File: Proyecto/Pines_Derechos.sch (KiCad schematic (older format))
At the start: 6 parts, among them U1 MAX7219, U2 MAX7219

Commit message: Avance de FootPrints
Se terminó diseño de esquemáticos en ojas Jerárquicas; se avanzó a un
70% en las referencias de FootPrint, y se actualizaron hojas de datos de
la Matriz de LEDs 8x8.
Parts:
- added M1: Matrix_8x8_LED, symbol Matrix_8x8_LED
- AFF1: footprint (none) -> FootPrints:Cx56-12
- R1, R2: footprint (none) -> FootPrints:R_0805_HandSoldering
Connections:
- net labels added: PF
- net labels removed: +3.3V
- wire segments 84 -> 95
- no-connect marks 30 -> 31
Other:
- note added: "Power Flag\ncon etiqueta global."

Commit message: Modelos 3D
Se modificaron FootPrints y se agregaron modelos en 3D.
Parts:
- AFF1: Desc (none) -> Character LED Display Module Red 7-Segment 4 Character Comm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; Digikey# (none) -> 67-1442-ND; Manf (none) -> Lumex Opto/Components Inc.; Manf# (none) -> LDQ-N514RI
- M1: footprint (none) -> FootPrints:Matrix_8x8_LEDs; Desc (none) -> Dot Matrix Display Module 8 x 8 Common Cathode Row, Common 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; Digikey# (none) -> TA15-11EWA-ND; Manf (none) -> Kingbright; Manf# (none) -> TA15-11EWA
- R1, R2: Desc (none) -> Resistencia en microprocesador 0.25 W, 1/4 W ±0.5% 9.53 k O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; Digikey# (none) -> P21131TR-ND; Manf (none) -> Panasonic Electronic Components; Manf# (none) -> ERJ-PB6D9531V
- U1, U2: footprint (none) -> FootPrints:MAX7219; Desc (none) -> IC DRIVER LED DISP 8DGT 24-SOIC; Digikey# (none) -> MAX7219CWG+-ND; Manf (none) -> Maxim Integrated; Manf# (none) -> MAX7219CWG+
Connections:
- net labels removed: PF
- wire segments 95 -> 94
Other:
- note added: "En los Integrados MAX7219:\nLos cátodos son - DIG0 al DIG 7.\nLos ánodos son SEGa al SEGg y SEGdp"
- note removed: "Power Flag\ncon etiqueta global."
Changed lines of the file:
@@
 F 0 "U1" H 2350 3600 50  0000 C CNN
 F 1 "MAX7219" H 3050 3600 50  0000 C CNN
-F 2 "" H 2750 2800 50  0001 C CNN
-F 3 "" H 2750 2800 50  0001 C CNN
+F 2 "FootPrints:MAX7219" H 2750 2800 50  0001 C CNN
+F 3 "MAX7219,21" H 2750 2800 50  0001 C CNN
+F 4 "Maxim Integrated" H 2750 2800 60  0001 C CNN "Manf"
+F 5 "MAX7219CWG+" H 2750 2800 60  0001 C CNN "Manf#"
+F 6 "MAX7219CWG+-ND" H 2750 2800 60  0001 C CNN "Digikey#"
+F 7 "IC DRIVER LED DISP 8DGT 24-SOIC" H 2750 2800 60  0001 C CNN "Desc"
 	1    2750 2800
 	1    0    0    -1
@@
 F 1 "9.53k" V 4050 2850 50  0000 C CNN
 F 2 "FootPrints:R_0805_HandSoldering" V 3980 2850 50  0001 C CNN
-F 3 "" H 4050 2850 50  0001 C CNN
+F 3 "Fixed Resistors Prod Catalog" H 4050 2850 50  0001 C CNN
+F 4 "Panasonic Electronic Components" V 4050 2850 60  0001 C CNN "Manf"
+F 5 "ERJ-PB6D9531V" V 4050 2850 60  0001 C CNN "Manf#"
+F 6 "P21131TR-ND" V 4050 2850 60  0001 C CNN "Digikey#"
+F 7 "Resistencia en microprocesador 0.25 W, 1/4 W ±0.5% 9.53 k Ohm AEC-Q200 automotriz, protección contra impulsos Película gruesa 0805 (2012 métrico)" V 4050 2850 60  0001 C CNN "Desc"
 	1    4050 2850
 	0    1    1    0
@@
 F 1 "CA56-12" H 2800 5950 50  0000 C CNN
 F 2 "FootPrints:Cx56-12" H 2250 5250 50  0001 C CNN
-F 3 "" H 2250 5250 50  0001 C CNN
+F 3 "LDQ-N514RI" H 2250 5250 50  0001 C CNN
+F 4 "Lumex Opto/Components Inc." H 2750 5250 60  0001 C CNN "Manf"
+F 5 "LDQ-N514RI" H 2750 5250 60  0001 C CNN "Manf#"
+F 6 "67-1442-ND" H 2750 5250 60  0001 C CNN "Digikey#"
+F 7 "Character LED Display Module Red 7-Segment 4 Character Common Cathode 2V 10mA 0.748\" H x 1.980\" W x 0.315\" D (19.00mm x 50.30mm x 8.00mm) 12-DIP (0.600\", 15.24mm)" H 2750 5250 60  0001 C CNN "Desc"
 	1    2750 5250
 	1    0    0    -1
@@
 F 0 "U2" H 8500 3500 50  0000 C CNN
 F 1 "MAX7219" H 9200 3500 50  0000 C CNN
-F 2 "" H 8900 2700 50  0001 C CNN
-F 3 "" H 8900 2700 50  0001 C CNN
+F 2 "FootPrints:MAX7219" H 8900 2700 50  0001 C CNN
+F 3 "MAX7219,21" H 8900 2700 50  0001 C CNN
+F 4 "Maxim Integrated" H 8900 2700 60  0001 C CNN "Manf"
+F 5 "MAX7219CWG+" H 8900 2700 60  0001 C CNN "Manf#"
+F 6 "MAX7219CWG+-ND" H 8900 2700 60  0001 C CNN "Digikey#"
+F 7 "IC DRIVER LED DISP 8DGT 24-SOIC" H 8900 2700 60  0001 C CNN "Desc"
 	1    8900 2700
 	1    0    0    -1
@@
 F 1 "9.53k" V 10200 2750 50  0000 C CNN
 F 2 "FootPrints:R_0805_HandSoldering" V 10130 2750 50  0001 C CNN
-F 3 "" H 10200 2750 50  0001 C CNN
+F 3 "Fixed Resistors Prod Catalog" H 10200 2750 50  0001 C CNN
+F 4 "Panasonic Electronic Components" V 10200 2750 60  0001 C CNN "Manf"
+F 5 "ERJ-PB6D9531V" V 10200 2750 60  0001 C CNN "Manf#"
+F 6 "P21131TR-ND" V 10200 2750 60  0001 C CNN "Digikey#"
+F 7 "Resistencia en microprocesador 0.25 W, 1/4 W ±0.5% 9.53 k Ohm AEC-Q200 automotriz, protección contra impulsos Película gruesa 0805 (2012 métrico)" V 10200 2750 60  0001 C CNN "Desc"
 	1    10200 2750
 	0    1    1    0
@@
 L GND #PWR?
 U 1 1 59275BE8
-P 6100 7000
+P 6100 6850
 AR Path="/59275BE8" Ref="#PWR?"  Part="1"
 AR Path="/5926FB74/59275BE8" Ref="#PWR06"  Part="1"
-F 0 "#PWR06" H 6100 6750 50  0001 C CNN
-F 1 "GND" H 5950 6950 50  0000 C CNN
-F 2 "" H 6100 7000 50  0001 C CNN
-F 3 "" H 6100 7000 50  0001 C CNN
-	1    6100 7000
+F 0 "#PWR06" H 6100 6600 50  0001 C CNN
+F 1 "GND" H 5950 6800 50  0000 C CNN
+F 2 "" H 6100 6850 50  0001 C CNN
+F 3 "" H 6100 6850 50  0001 C CNN
+	1    6100 6850
 	1    0    0    -1
 $EndComp
@@
 Entry Wire Line
 	7450 3150 7550 3050
-Text Label 6100 6850 2    60   ~ 0
-GND
-Wire Wire Line
-	6100 6850 6100 7000
-Wire Notes Line
-	5750 6600 6350 6600
-Wire Notes Line
-	6350 6600 6350 7300
-Wire Notes Line
-	6350 7300 5750 7300
-Wire Notes Line
-	5750 7300 5750 6600
-Wire Notes Line
-	5750 7300 5550 7500
-Wire Notes Line
-	5550 7500 5400 7500
-Text Notes 4250 7600 0    60   ~ 0
+Wire Wire Line
+	6100 6700 6100 6850
+Wire Notes Line
+	5750 6450 6350 6450
+Wire Notes Line
+	6350 6450 6350 7150
+Wire Notes Line
+	6350 7150 5750 7150
+Wire Notes Line
+	5750 7150 5750 6450
+Wire Notes Line
+	5750 7150 5550 7350
+Wire Notes Line
+	5550 7350 5400 7350
+Text Notes 4250 7450 0    60   ~ 0
 GND con etiqueta global\npara el MAX7219 de la \nmatriz de LEDs
 NoConn ~ 5300 2800
@@
 F 0 "M1" H 8150 6000 60  0000 C CNN
 F 1 "Matrix_8x8_LED" H 9350 6000 60  0000 C CNN
-F 2 "" H 8850 5150 60  0001 C CNN
+F 2 "FootPrints:Matrix_8x8_LEDs" H 8850 5150 60  0001 C CNN
 F 3 "TA15-11EWA" H 8850 5150 60  0001 C CNN
+F 4 "Kingbright" H 8900 5150 60  0001 C CNN "Manf"
+F 5 "TA15-11EWA" H 8900 5150 60  0001 C CNN "Manf#"
+F 6 "TA15-11EWA-ND" H 8900 5150 60  0001 C CNN "Digikey#"
+F 7 "Dot Matrix Display Module 8 x 8 Common Cathode Row, Common Anode Column Red 2V 1.50\" L x 1.50\" W x 0.41\" H (38.1mm x 38.1mm x 10.4mm)" H 8900 5150 60  0001 C CNN "Desc"
 	1    8900 5150
 	1    0    0    -1
@@
 Wire Wire Line
 	10050 2750 9650 2750
-$Comp
-L PWR_FLAG #FLG07
-U 1 1 592A4183
-P 3100 6950
-F 0 "#FLG07" H 3100 7025 50  0001 C CNN
-F 1 "PWR_FLAG" H 3100 7100 50  0000 C CNN
-F 2 "" H 3100 6950 50  0001 C CNN
-F 3 "" H 3100 6950 50  0001 C CNN
-	1    3100 6950
-	1    0    0    -1
-$EndComp
 Wire Wire Line
 	4250 2850 4250 2700
-Text Label 3100 7150 1    60   ~ 0
-PF
-Wire Wire Line
-	3100 7150 3100 6950
-Wire Notes Line
-	2800 6650 3400 6650
-Wire Notes Line
-	3400 6650 3400 7300
-Wire Notes Line
-	3400 7300 2800 7300
-Wire Notes Line
-	2800 7300 2800 6650
-Text Notes 2350 7550 2    60   ~ 0
-Power Flag\ncon etiqueta global.
-Wire Notes Line
-	2650 7450 2450 7450
-Wire Notes Line
-	2800 7300 2650 7450
-Text Label 3650 2850 0    60   ~ 0
-PF
-Text Label 9800 2750 0    60   ~ 0
-PF
 NoConn ~ 5300 1300
-Text Label 6100 6950 0    60   ~ 0
-PF
 Wire Wire Line
 	6900 1300 6500 1300
 $Comp
-L +5V #PWR08
+L +5V #PWR07
 U 1 1 592A66C3
 P 6900 1200
-F 0 "#PWR08" H 6900 1050 50  0001 C CNN
+F 0 "#PWR07" H 6900 1050 50  0001 C CNN
 F 1 "+5V" H 6890 1380 50  0000 C CNN
 F 2 "" H 6900 1200 50  0001 C CNN
@@
 Wire Wire Line
 	6900 1200 6900 1300
+Text Notes 950  1250 0    79   ~ 0
+En los Integrados MAX7219:\nLos cátodos son - DIG0 al DIG 7.\nLos ánodos son SEGa al SEGg y SEGdp
+Wire Notes Line
+	750  700  3500 700
+Wire Notes Line
+	3500 700  3500 1450
+Wire Notes Line
+	3500 1450 750  1450
+Wire Notes Line
+	750  1450 750  700
+Text Label 6100 6700 2    60   ~ 0
+GND
 $EndSCHEMATC

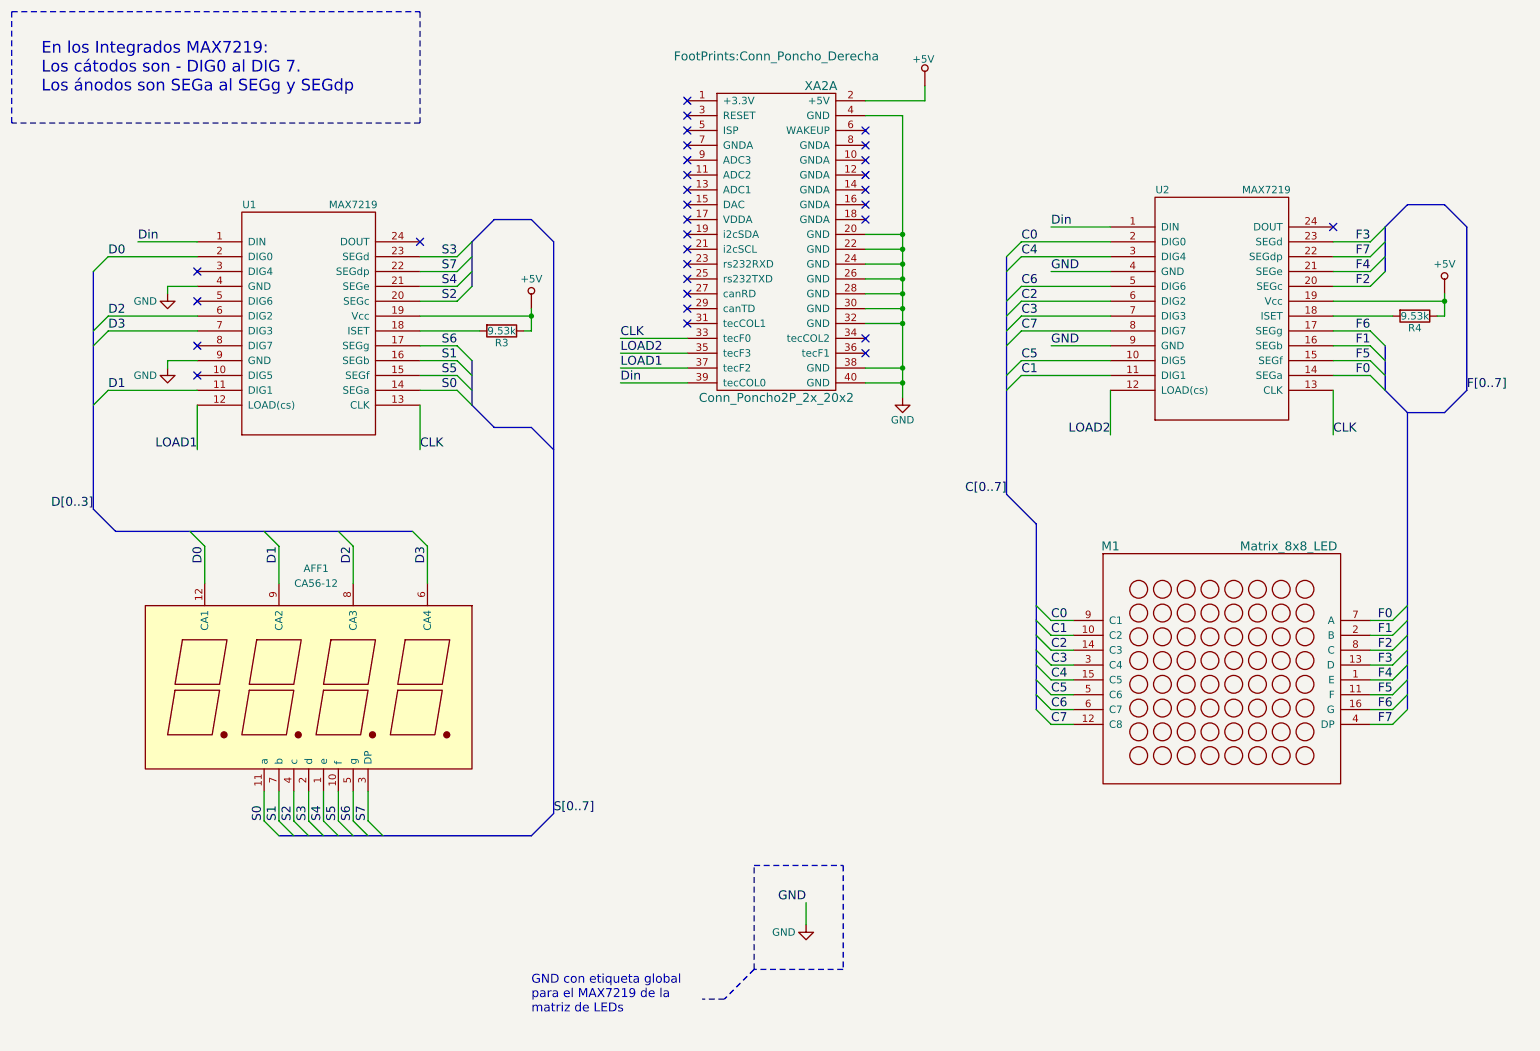
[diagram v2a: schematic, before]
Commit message: Ruteo y 3D
Se realizó el ruteo completo y se agregaron modelos 3D
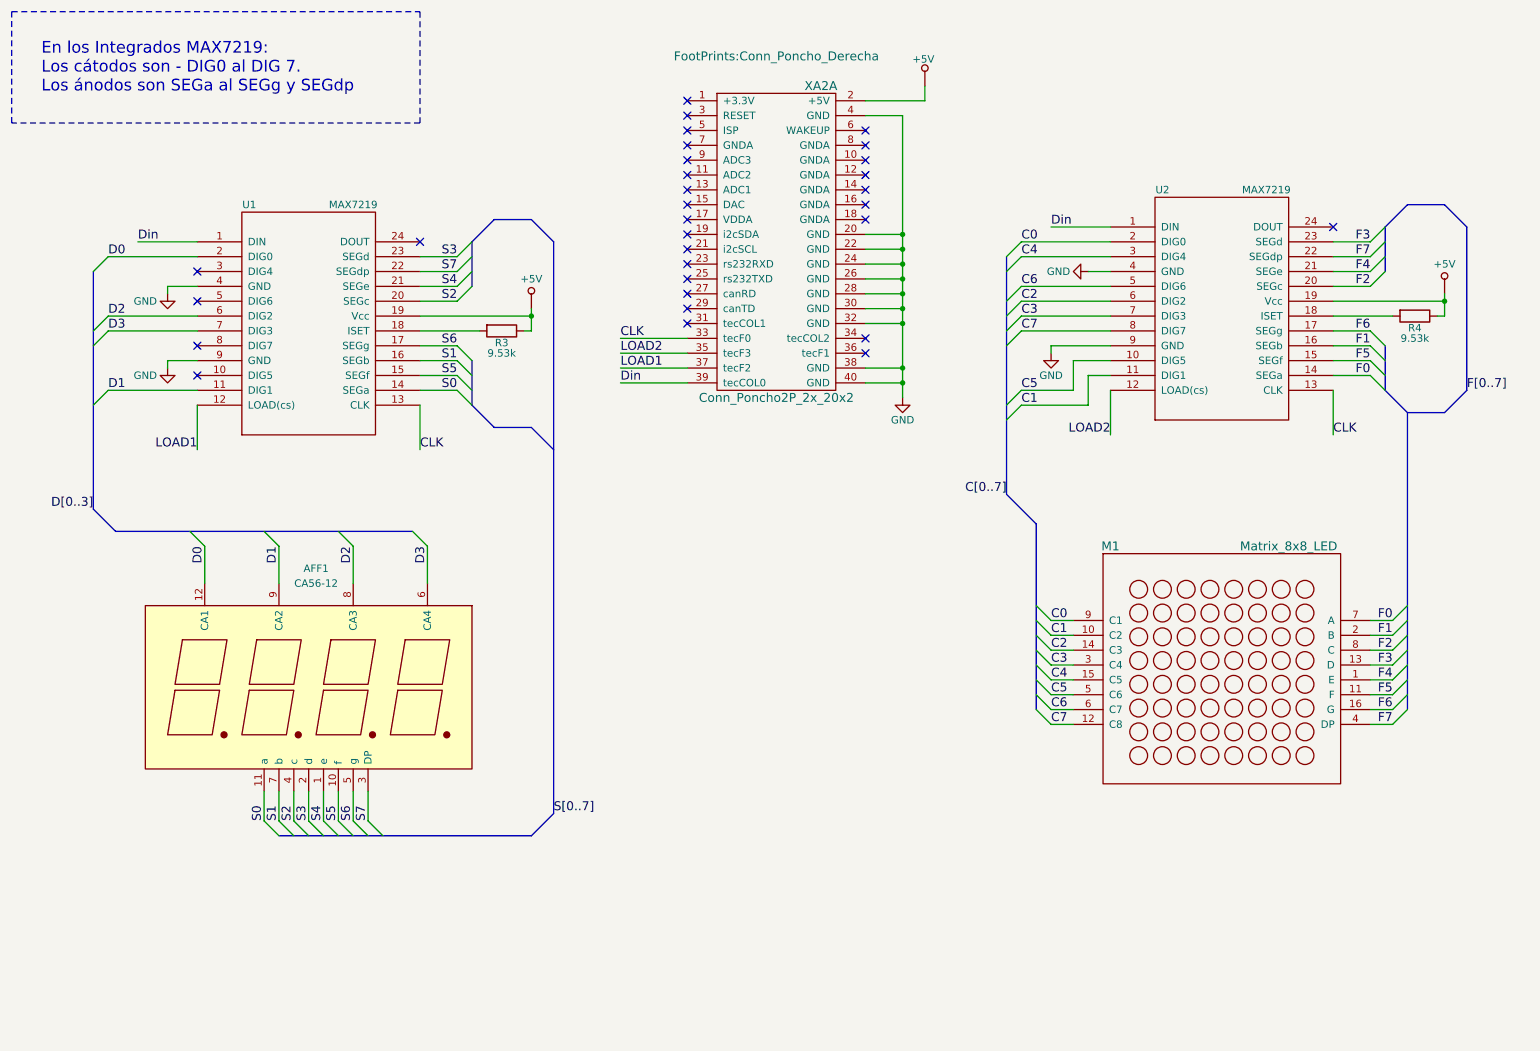
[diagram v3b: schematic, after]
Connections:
- net GND: no longer names the net of U2.4 (GND)
- net GND: no longer U2.9 (GND)
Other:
- note removed: "GND con etiqueta global\npara el MAX7219 de la \nmatriz de LEDs"
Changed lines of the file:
@@
 LIBS:display
 LIBS:Poncho_Esqueleto
+LIBS:conn
 LIBS:Poncho_Educativo_v2.0-cache
 EELAYER 25 0
@@
 Date "2017-05-25"
 Rev ""
-Comp "Curso - Diseño de PCB"
-Comment1 "Autor Esquemático: Ing. Jhon Jairo Vargas Yaya"
-Comment2 ""
-Comment3 ""
-Comment4 ""
+Comp "CESE - Diseño de PCB"
+Comment1 "Licencia del proyecto: BSD 2 - Archivo: LICENSE"
+Comment2 "Autor del Poncho: Ing. Jhon Jairo Vargas Yaya"
+Comment3 "Autores y Licencia del template (Diego Brengi - UNLaM)"
+Comment4 "Revisor: Juan Carlos Suarez"
 $EndDescr
 $Comp
@@
 AR Path="/5926FB74/59273456" Ref="R3"  Part="1"
 F 0 "R3" V 4130 2850 50  0000 C CNN
-F 1 "9.53k" V 4050 2850 50  0000 C CNN
+F 1 "9.53k" V 4200 2850 50  0000 C CNN
 F 2 "FootPrints:R_0805_HandSoldering" V 3980 2850 50  0001 C CNN
 F 3 "Fixed Resistors Prod Catalog" H 4050 2850 50  0001 C CNN
@@
 AR Path="/5926FB74/59275BDA" Ref="R4"  Part="1"
 F 0 "R4" V 10280 2750 50  0000 C CNN
-F 1 "9.53k" V 10200 2750 50  0000 C CNN
+F 1 "9.53k" V 10350 2750 50  0000 C CNN
 F 2 "FootPrints:R_0805_HandSoldering" V 10130 2750 50  0001 C CNN
 F 3 "Fixed Resistors Prod Catalog" H 10200 2750 50  0001 C CNN
@@
 	0    1    1    0
 $EndComp
-$Comp
-L GND #PWR?
-U 1 1 59275BE8
-P 6100 6850
-AR Path="/59275BE8" Ref="#PWR?"  Part="1"
-AR Path="/5926FB74/59275BE8" Ref="#PWR06"  Part="1"
-F 0 "#PWR06" H 6100 6600 50  0001 C CNN
-F 1 "GND" H 5950 6800 50  0000 C CNN
-F 2 "" H 6100 6850 50  0001 C CNN
-F 3 "" H 6100 6850 50  0001 C CNN
-	1    6100 6850
-	1    0    0    -1
-$EndComp
 Text Label 7550 2250 0    60   ~ 0
 C0
-Text Label 7550 3150 0    60   ~ 0
+Text Label 7550 3350 0    60   ~ 0
 C1
 Text Label 7550 2750 0    60   ~ 0
@@
 	8150 2250 7550 2250
 Wire Wire Line
-	8150 3150 7550 3150
-Wire Wire Line
 	8150 2650 7550 2650
 Wire Wire Line
@@
 Entry Wire Line
 	7450 2850 7550 2750
-Entry Wire Line
-	7450 3250 7550 3150
 Wire Bus Line
 	7450 3950 7450 2350
@@
 Wire Wire Line
 	9650 3250 9650 3550
-Text Label 7750 2450 0    60   ~ 0
-GND
-Text Label 7750 2950 0    60   ~ 0
-GND
 Text Label 7550 2350 0    60   ~ 0
 C4
@@
 Text Label 7550 2850 0    60   ~ 0
 C7
-Text Label 7550 3050 0    60   ~ 0
+Text Label 7550 3250 0    60   ~ 0
 C5
 Wire Wire Line
-	8150 3050 7550 3050
-Wire Wire Line
 	8150 2950 7750 2950
 Wire Wire Line
@@
 	8150 2550 7550 2550
 Wire Wire Line
-	8150 2450 7750 2450
-Wire Wire Line
 	8150 2350 7550 2350
 Entry Wire Line
@@
 Entry Wire Line
 	7450 2950 7550 2850
-Entry Wire Line
-	7450 3150 7550 3050
-Wire Wire Line
-	6100 6700 6100 6850
-Wire Notes Line
-	5750 6450 6350 6450
-Wire Notes Line
-	6350 6450 6350 7150
-Wire Notes Line
-	6350 7150 5750 7150
-Wire Notes Line
-	5750 7150 5750 6450
-Wire Notes Line
-	5750 7150 5550 7350
-Wire Notes Line
-	5550 7350 5400 7350
-Text Notes 4250 7450 0    60   ~ 0
-GND con etiqueta global\npara el MAX7219 de la \nmatriz de LEDs
 NoConn ~ 5300 2800
 NoConn ~ 5300 2700
@@
 	6900 1300 6500 1300
 $Comp
-L +5V #PWR07
+L +5V #PWR06
 U 1 1 592A66C3
 P 6900 1200
-F 0 "#PWR07" H 6900 1050 50  0001 C CNN
+F 0 "#PWR06" H 6900 1050 50  0001 C CNN
 F 1 "+5V" H 6890 1380 50  0000 C CNN
 F 2 "" H 6900 1200 50  0001 C CNN
@@
 Wire Notes Line
 	750  1450 750  700
-Text Label 6100 6700 2    60   ~ 0
-GND
+Wire Wire Line
+	8150 3150 8000 3150
+Wire Wire Line
+	8000 3150 8000 3350
+Wire Wire Line
+	8000 3350 7550 3350
+Entry Wire Line
+	7450 3450 7550 3350
+Wire Wire Line
+	8150 3050 7900 3050
+Wire Wire Line
+	7900 3050 7900 3250
+Wire Wire Line
+	7900 3250 7550 3250
+Entry Wire Line
+	7450 3350 7550 3250
+$Comp
+L GND #PWR07
+U 1 1 5968354F
+P 7750 3000
+F 0 "#PWR07" H 7750 2750 50  0001 C CNN
+F 1 "GND" H 7750 2850 50  0000 C CNN
+F 2 "" H 7750 3000 50  0001 C CNN
+F 3 "" H 7750 3000 50  0001 C CNN
+	1    7750 3000
+	1    0    0    -1
+$EndComp
+Wire Wire Line
+	7750 2950 7750 3000
+$Comp
+L GND #PWR08
+U 1 1 5968361C
+P 8000 2450
+F 0 "#PWR08" H 8000 2200 50  0001 C CNN
+F 1 "GND" V 8000 2250 50  0000 C CNN
+F 2 "" H 8000 2450 50  0001 C CNN
+F 3 "" H 8000 2450 50  0001 C CNN
+	1    8000 2450
+	0    1    1    0
+$EndComp
+Wire Wire Line
+	8150 2450 8000 2450
 $EndSCHEMATC
